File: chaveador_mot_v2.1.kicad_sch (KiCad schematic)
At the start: 6 parts, among them Q1 IRF9540N, U1 4N25

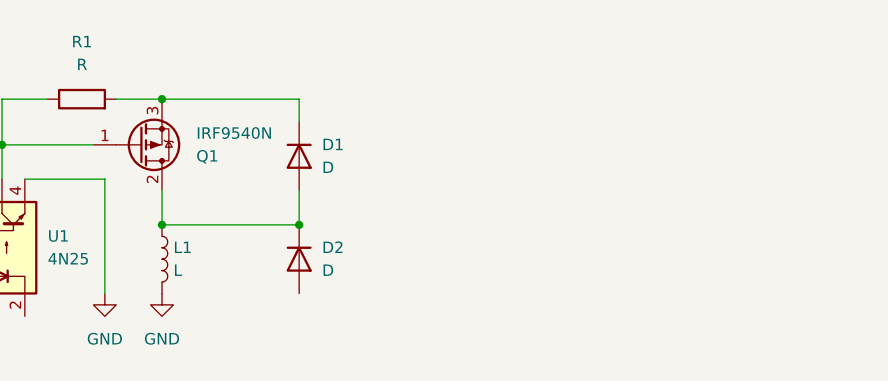
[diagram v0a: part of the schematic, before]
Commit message: Adicionei as fontes de alimentação Vcc = 18v e Vcn24 = -24
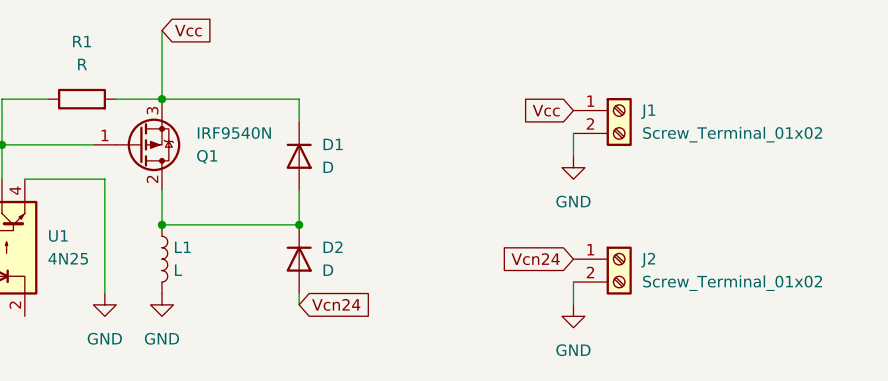
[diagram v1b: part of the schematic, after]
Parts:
- added J1, J2: Screw_Terminal_01x02, symbol Connector:Screw_Terminal_01x02
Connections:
- net GND: now also J1.2 (Pin_2), J2.2 (Pin_2)
- net Vcc: now reaches D1.1 (K), Q1.3 (S), R1.2
- net Vcc: now also J1.1 (Pin_1)
- net Vcn24: now reaches D2.2 (A)
- net Vcn24: now also J2.1 (Pin_1)

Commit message: Montei a primeira versão da pcb, adicionei footprints, e coloquei parafusos.
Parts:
- added H1, H2, H3, H4: MountingHole, MountingHole:MountingHole_2.5mm_Pad, symbol Mechanical:MountingHole
- D1, D2: footprint (none) -> Diode_THT:D_A-405_P10.16mm_Horizontal
- J1, J2, L1: footprint (none) -> TerminalBlock_Phoenix:TerminalBlock_Phoenix_MKDS-1,5-2_1x02_P5.00mm_Horizontal
- R1: footprint (none) -> Resistor_THT:R_Axial_DIN0207_L6.3mm_D2.5mm_P10.16mm_Horizontal

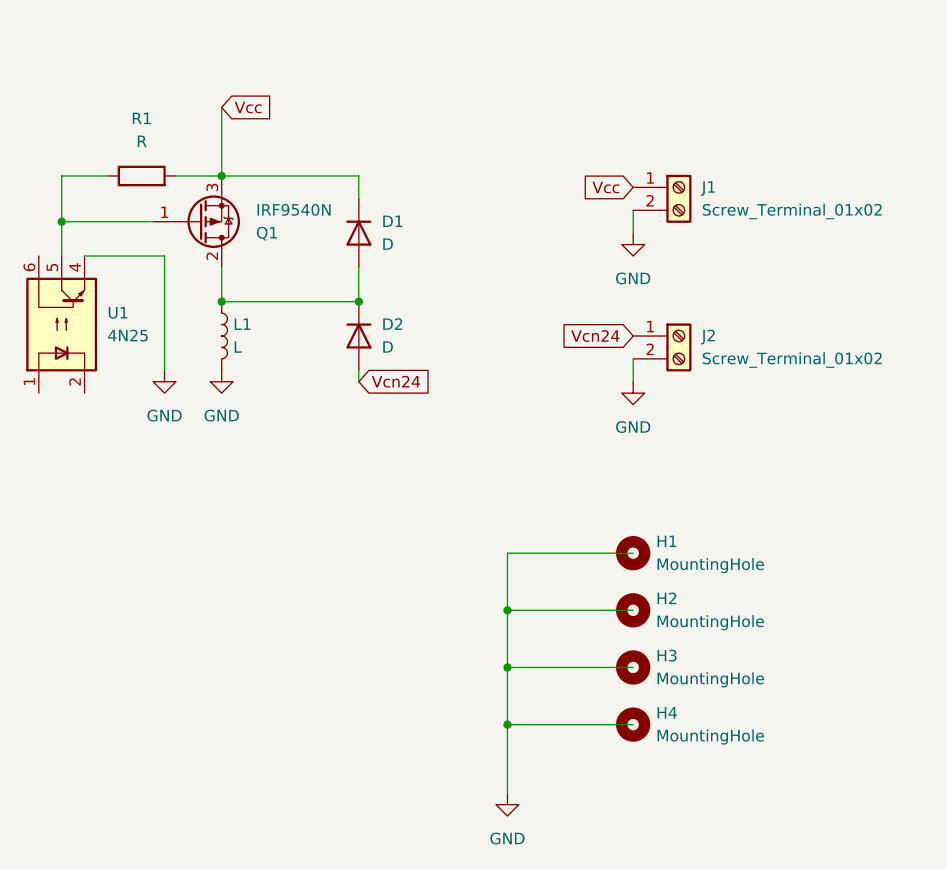
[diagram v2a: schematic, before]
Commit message: coloquei a entrada do sinal para o un425 e rearranjei a pcb para conctar tudo
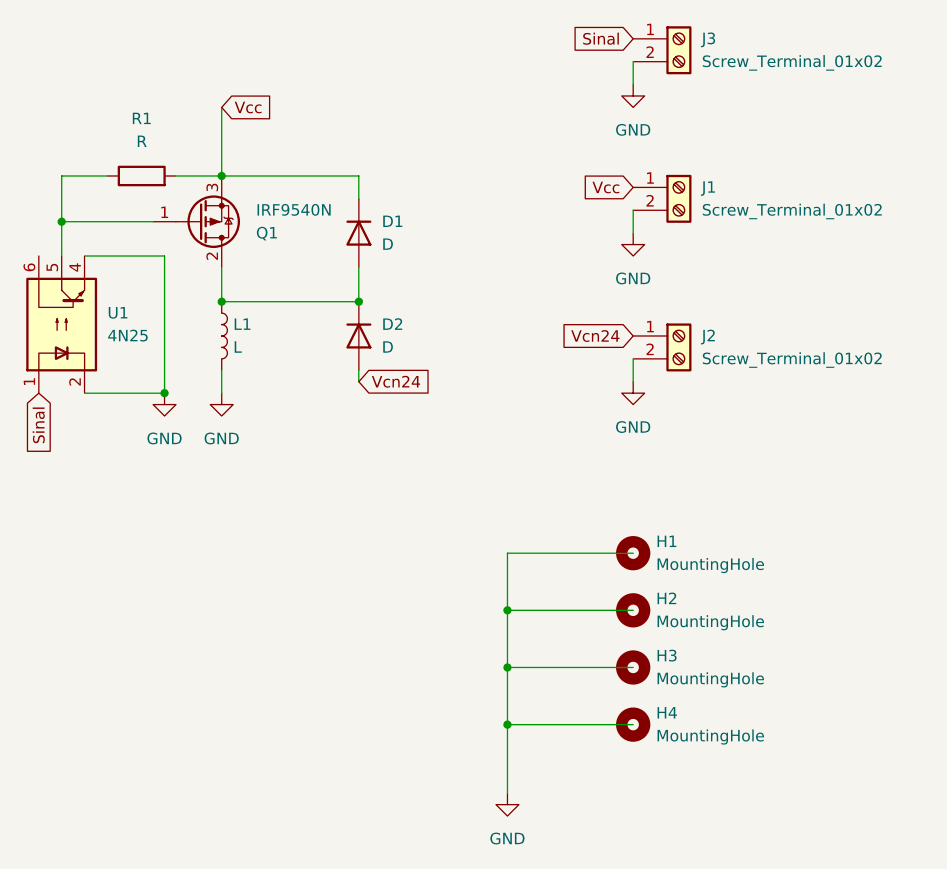
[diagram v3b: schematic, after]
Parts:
- added J3: Screw_Terminal_01x02, TerminalBlock_Phoenix:TerminalBlock_Phoenix_MKDS-1,5-2_1x02_P5.00mm_Horizontal, symbol Connector:Screw_Terminal_01x02
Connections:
- net GND: now also U1.2, J3.2 (Pin_2)
- net Sinal: now reaches U1.1
- net Sinal: now also J3.1 (Pin_1)

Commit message: Coloquei o valor de R1 e dos diodos.
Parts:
- D1, D2: value D -> 1N5408
- R1: value R -> 22k
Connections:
- net Vcc renamed Vcc24
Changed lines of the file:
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@@
 		)
 	)
-	(global_label "Vcc"
+	(global_label "Vcc24"
 		(shape input)
 		(at 140.97 72.39 180)
@@
 		)
 		(property "Intersheetrefs" "${INTERSHEET_REFS}"
-			(at 134.719 72.39 0)
+			(at 132.3 72.39 0)
 			(hide yes)
 			(show_name no)
@@
 		)
 	)
-	(global_label "Vcc"
+	(global_label "Vcc24"
 		(shape input)
 		(at 95.25 63.5 0)
@@
 		)
 		(property "Intersheetrefs" "${INTERSHEET_REFS}"
-			(at 101.501 63.5 0)
+			(at 103.92 63.5 0)
 			(hide yes)
 			(show_name no)
@@
 			)
 		)
-		(property "Value" "D"
+		(property "Value" "1N5408"
 			(at 113.03 78.7399 90)
 			(show_name no)
@@
 			)
 		)
-		(property "Value" "R"
+		(property "Value" "22k"
 			(at 86.36 67.31 90)
 			(show_name no)
@@
 			)
 		)
-		(property "Value" "D"
+		(property "Value" "1N5408"
 			(at 113.03 90.1699 90)
 			(show_name no)

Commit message: Troquei o valor do mosfet para o que estamos realmente usando.
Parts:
- Q1: value IRF9540N -> IRF9640N
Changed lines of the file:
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@@
 			)
 		)
-		(property "Value" "IRF9540N"
+		(property "Value" "IRF9640N"
 			(at 99.06 74.9301 0)
 			(show_name no)

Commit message: Consertei o valor do mosfet.
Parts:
- Q1: value IRF9640N -> IRF9640
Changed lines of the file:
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@@
 			)
 		)
-		(property "Value" "IRF9640N"
+		(property "Value" "IRF9640"
 			(at 99.06 74.9301 0)
 			(show_name no)
